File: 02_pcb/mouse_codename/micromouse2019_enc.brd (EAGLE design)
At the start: 5.8 x 9.8 mm, 5 parts, among them IC1 AS5047D-ATSM

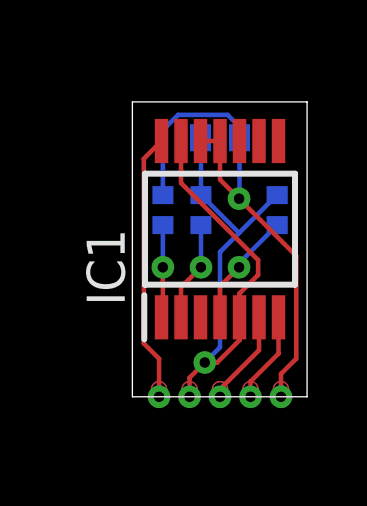
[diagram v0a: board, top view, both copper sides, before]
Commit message: Updated enc pcb, spi connector added
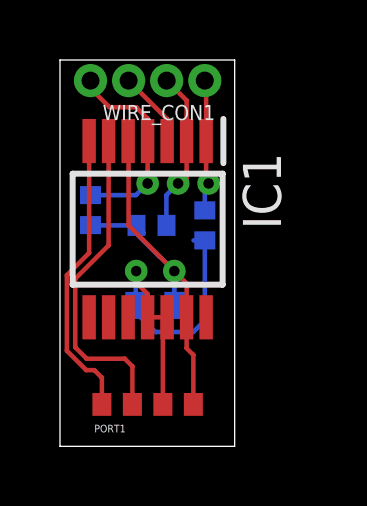
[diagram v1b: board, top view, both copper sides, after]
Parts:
- added PORT1: ENC_PORT_MODULE, parts_not_managed:ENC_PORT_MODULE
- added WIRE_CON1: CON_WIRE, parts_not_managed:PINHD4-1.27
- moved R3 6.22 mm to (21.1, 59.1), turned to 90 degrees
- moved C1 5.99 mm to (23.2, 55.9), turned to 180 degrees
- moved IC1 2.41 mm to (23.0, 58.4), turned to 270 degrees
- moved R2 1.73 mm to (23.1, 58.5), turned to 180 degrees
- moved R1 1.49 mm to (24.9, 58.5), turned to 270 degrees
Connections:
- removed net I: IC1.14
- removed net N$1: IC1.1, R1.1
- removed net N$2: IC1.2, R2.2
- removed net N$3: IC1.4, R3.2
- new net CLK: IC1.2, R2.2, WIRE_CON1.P2
- new net CSN: IC1.1, R1.1, WIRE_CON1.P1
- new net MISO: IC1.3, WIRE_CON1.P3
- new net MOSI: IC1.4, R3.2, WIRE_CON1.P4
- net +3V3: now also PORT1.P3
- net A: now also PORT1.P2
- net B: now also PORT1.P1
- net GND: now also PORT1.P4
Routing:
- net I: track 8.98 -> 0.00 mm, vias 1 -> 0
- net A: track 3.19 -> 10.8 mm, vias 1 -> 0
- net MOSI: track 0.00 -> 6.80 mm, vias 0 -> 1
- net B: track 3.04 -> 9.73 mm, vias 1 -> 0
- net GND: track 21.1 -> 14.8 mm, vias 2 -> 1
- net CLK: track 0.00 -> 5.50 mm, vias 0 -> 1
- net +3V3: track 17.9 -> 12.5 mm, vias 2 -> 1
- net CSN: track 0.00 -> 4.49 mm, vias 0 -> 1
- net N$3: track 3.86 -> 0.00 mm, vias 1 -> 0
- net N$2: track 3.35 -> 0.00 mm, vias 1 -> 0
- net N$1: track 3.09 -> 0.00 mm, vias 1 -> 0
- net MISO: track 0.00 -> 2.55 mm
- removed copper zone on layer 1, net +3V3
- removed copper zone on layer 16, net +3V3
- removed copper zone on layer 1, net A
- removed copper zone on layer 16, net A
- removed copper zone on layer 1, net B
- removed copper zone on layer 16, net B
- removed copper zone on layer 1, net GND
- removed copper zone on layer 16, net GND
- removed copper zone on layer 1, net I
- removed copper zone on layer 16, net I
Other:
- board size 5.8 x 9.8 mm -> 5.8 x 12.9 mm

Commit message: enc PCB with correct measures
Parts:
- moved C1 56.6 mm to (3.21, 2.94)
- moved R1 56.6 mm to (4.86, 5.61)
- moved R2 56.6 mm to (3.08, 5.61)
- moved R3 56.6 mm to (1.05, 6.11)
- moved WIRE_CON1 56.6 mm to (2.95, 10.4)
- moved IC1 56.6 mm to (2.95, 5.51)
- moved PORT1 55.9 mm to (2.95, 0.38)
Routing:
- net +3V3: track 12.5 -> 11.7 mm
- net GND: track 14.8 -> 14.1 mm
- net A: track 10.8 -> 10.1 mm
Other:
- board size 5.8 x 12.9 mm -> 5.9 x 11.1 mm
